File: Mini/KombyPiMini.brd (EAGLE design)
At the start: 63.2 x 21.6 mm, 5 parts

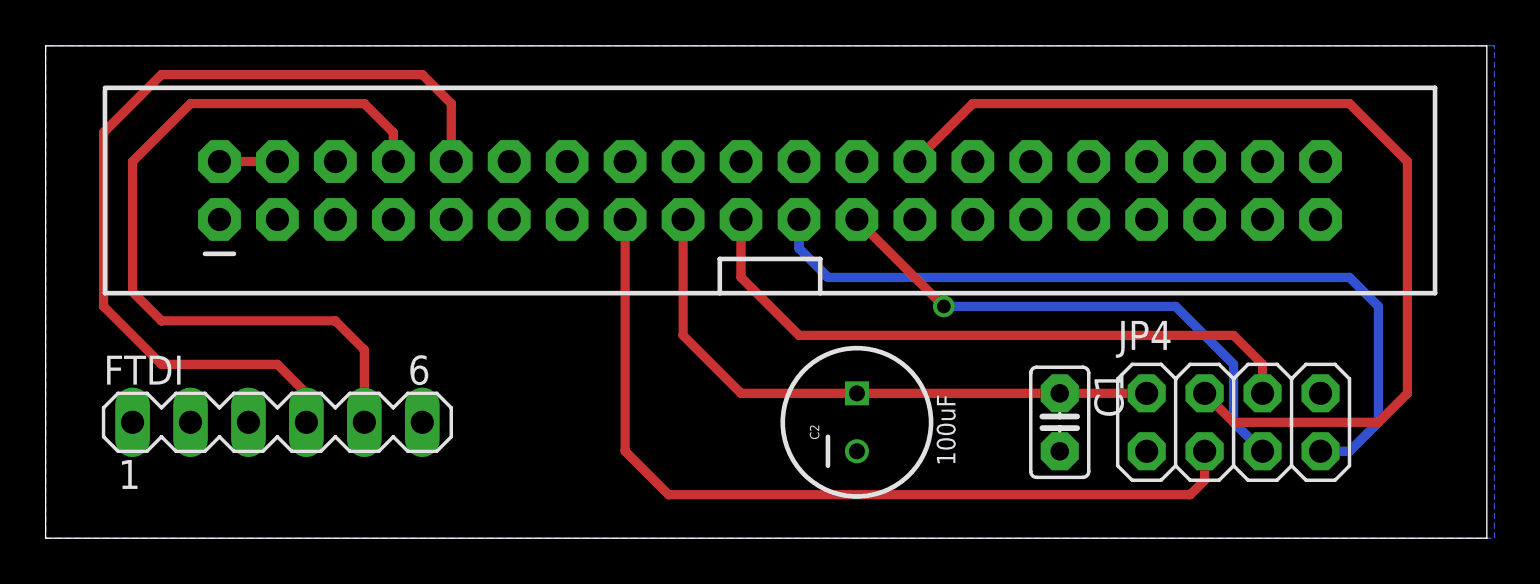
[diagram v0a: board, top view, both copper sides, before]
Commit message: Update KombyPiMini with properly oriented nRF
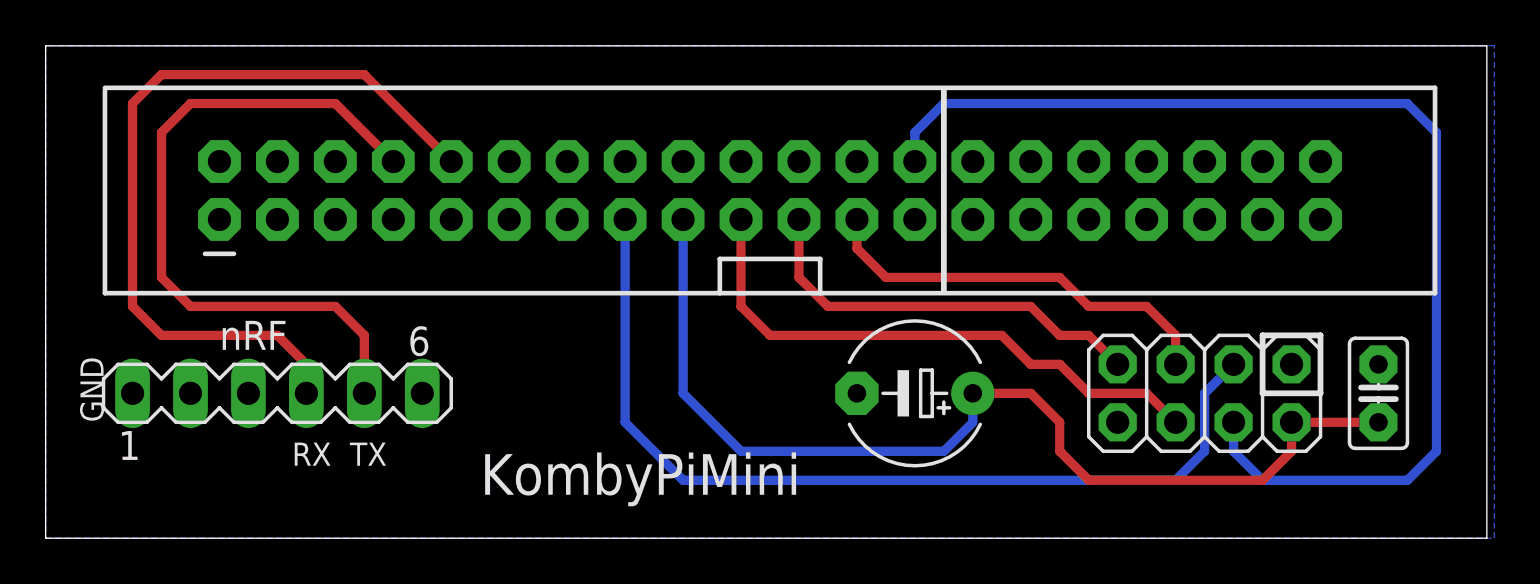
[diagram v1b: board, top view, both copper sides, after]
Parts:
- C2: device SparkFun:CPOL-RADIAL-100UF-25V -> rcl:E5-6
- moved C1 14.0 mm to (58.4, 6.35), turned to 90 degrees
- moved C2 2.84 mm to (38.1, 6.35), turned to 180 degrees
- moved JP4 1.80 mm to (50.8, 6.35), turned to 180 degrees
- moved FTDI 1.27 mm to (10.2, 6.35)
- renumbered JP3 to JP2
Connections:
- net 3.3V: now also C2.+; no longer C2.1
- net GND: now also C2.-; no longer C2.2
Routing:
- net 3.3V: track 26.5 -> 45.1 mm
- net MISO: track 35.9 -> 18.1 mm
- net CE1: track 43.8 -> 50.4 mm
- net SCLK: track 23.5 -> 18.1 mm, vias 1 -> 0
- net TXO: track 34.4 -> 30.6 mm
- net RXI: track 38.7 -> 34.9 mm
- net MOSI: track 28.2 -> 25.0 mm
- net VCC: track 2.54 -> 0.00 mm
- net RF_CE: track 37.9 -> 40.2 mm
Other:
- board text added: "(c) 2015 Mat Mrosko"
- board text added: "GND"
- board text added: "KombyPiMini"
- board text added: "RX"
- board text added: "TX"
- board text added: "nRF"
